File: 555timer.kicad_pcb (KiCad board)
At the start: 4 copper layers, 10 parts, among them U1 NE555P

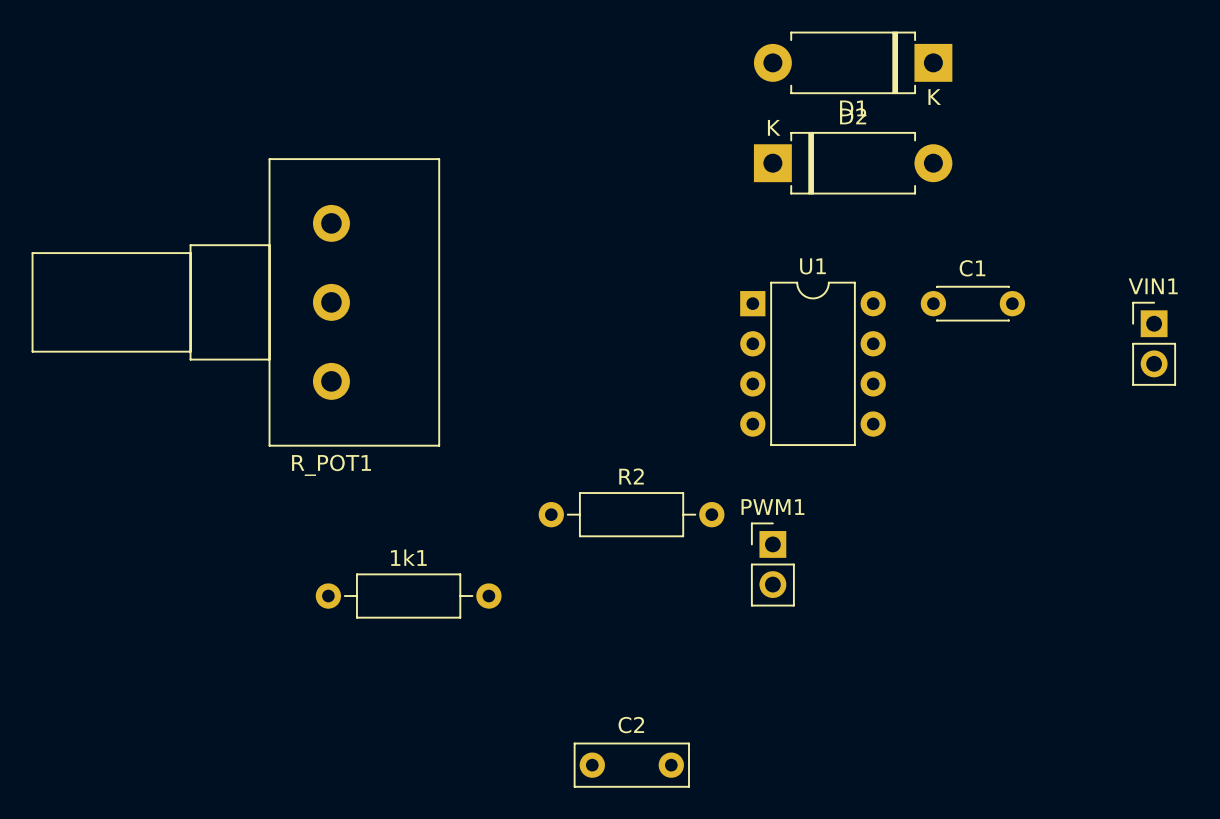
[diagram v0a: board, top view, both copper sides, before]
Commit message: Set the componnets and created a pcb rectangle
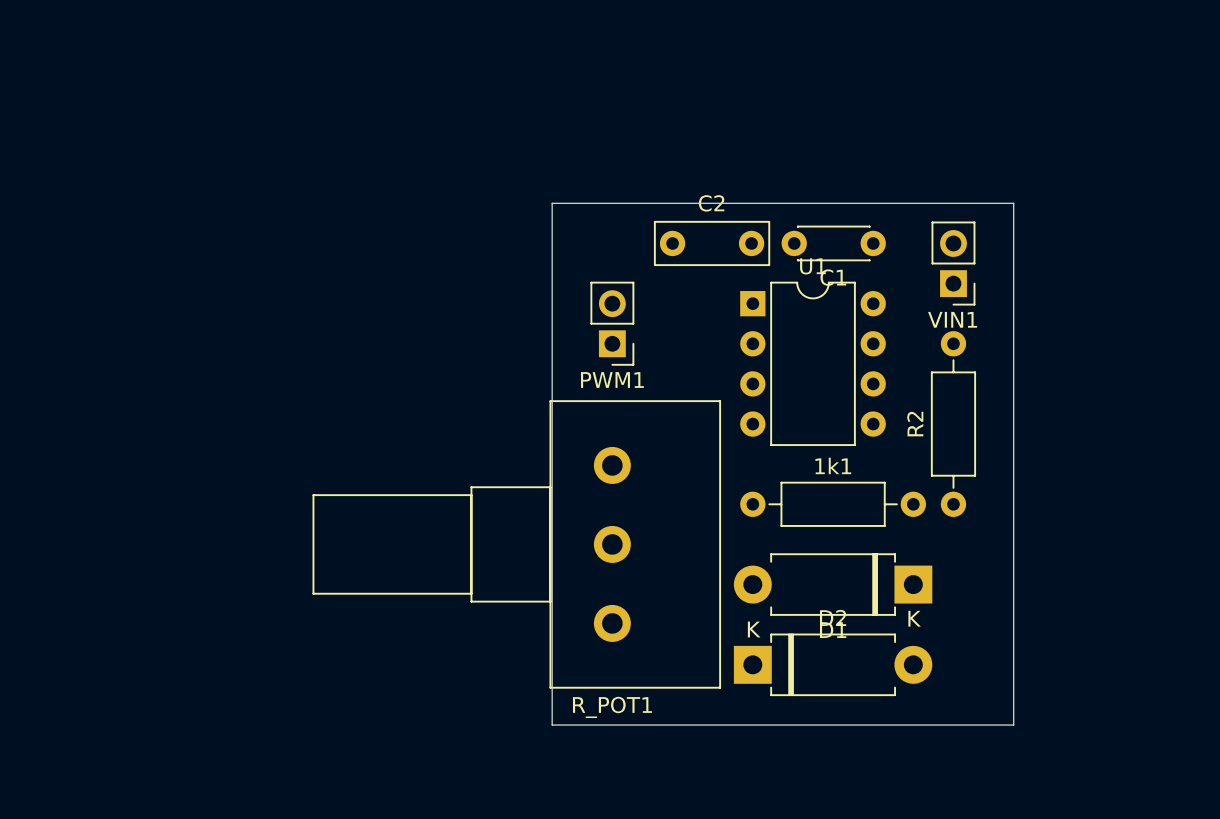
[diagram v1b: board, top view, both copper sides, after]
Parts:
- moved C2 33.4 mm to (146.1, 88.9)
- moved D1 33.0 mm to (161.3, 110.5)
- moved D2 31.8 mm to (151.1, 115.6)
- moved 1k1 27.5 mm to (151.1, 105.4)
- moved R2 25.5 mm to (163.8, 105.4), turned to 90 degrees
- moved R_POT1 23.5 mm to (142.2, 103.0)
- moved PWM1 16.3 mm to (142.2, 95.2), turned to 180 degrees
- moved VIN1 13.0 mm to (163.8, 91.4), turned to 180 degrees
- moved C1 5.39 mm to (158.8, 88.9), turned to 180 degrees
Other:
- board outline added: 29.2 x 33 mm

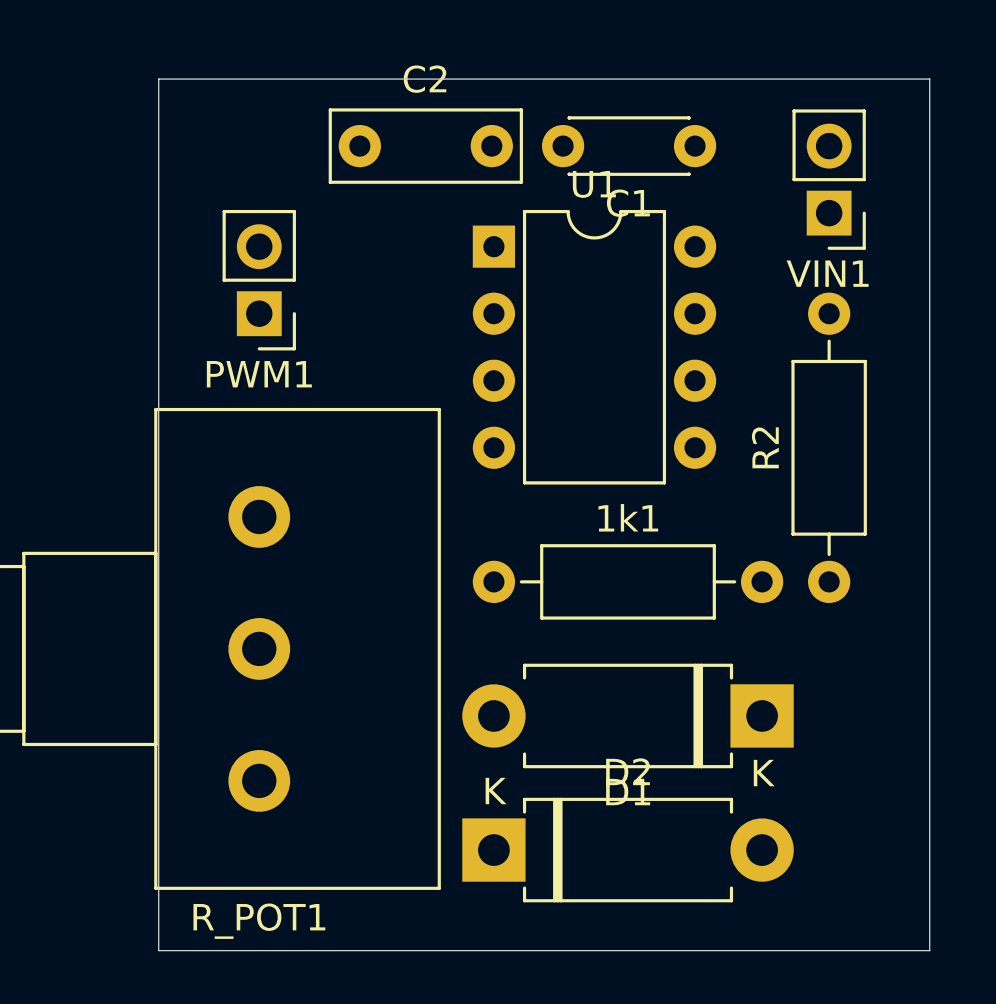
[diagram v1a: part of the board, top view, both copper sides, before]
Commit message: Rounded the corners
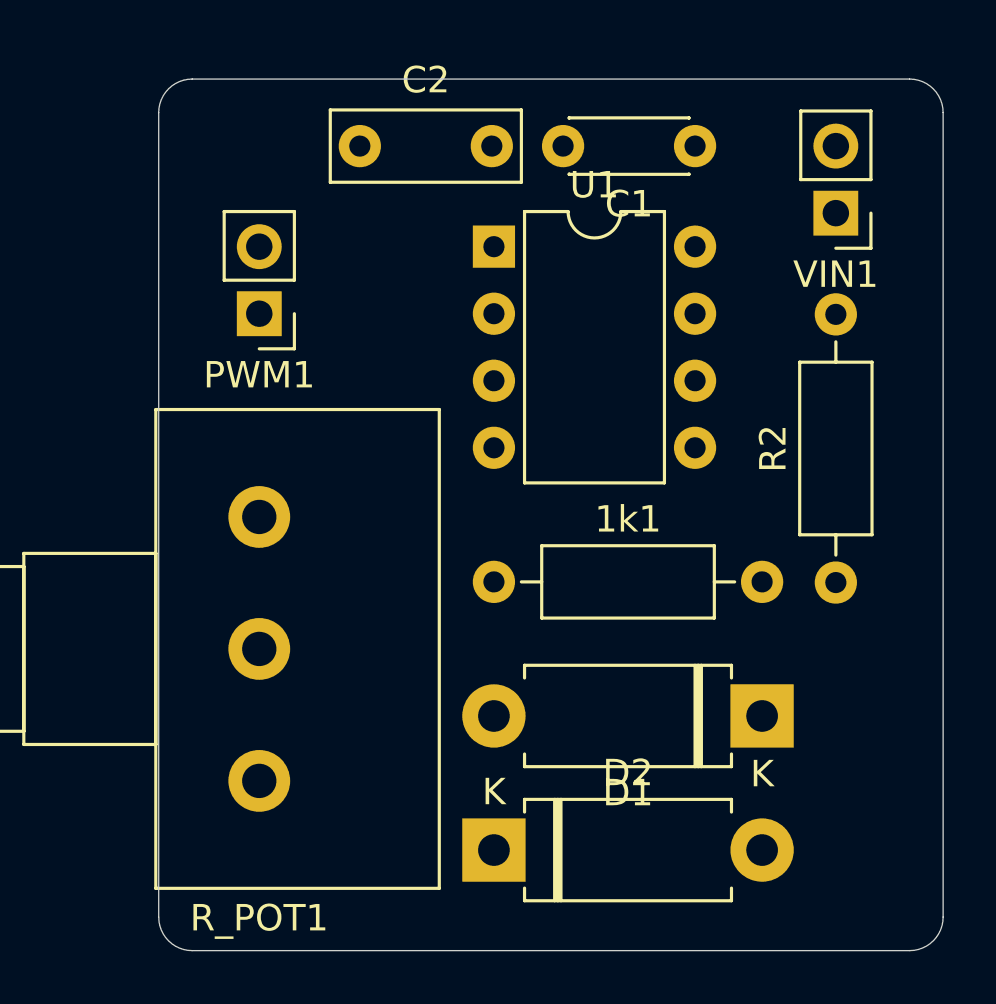
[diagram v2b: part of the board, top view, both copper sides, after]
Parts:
- moved R2 0.26 mm to (164.1, 105.4)
- moved VIN1 0.25 mm to (164.1, 91.4)
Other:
- board size 29.2 x 33 mm -> 29.7 x 33 mm
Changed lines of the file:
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@@
   (general
     (thickness 1.6002)
-    (drawings 4)
+    (drawings 8)
     (tracks 0)
     (zones 0)
@@
   )
   (module Connector_PinHeader_2.54mm:PinHeader_1x02_P2.54mm_Vertical (layer Front)
-    (at 163.83 91.44 180)
+    (at 164.084 91.44 180)
     (descr "Through hole straight pin header, 1x02, 2.54mm pitch, single row")
     (tags "Through hole pin header THT 1x02 2.54mm single row")
@@
   )
   (module Resistor_THT:R_Axial_DIN0207_L6.3mm_D2.5mm_P10.16mm_Horizontal (layer Front)
-    (at 163.83 105.41 90)
+    (at 164.084 105.4354 90)
     (descr "Resistor, Axial_DIN0207 series, Axial, Horizontal, pin pitch=10.16mm, 0.25W = 1/4W, length*diameter=6.3*2.5mm^2, http://cdn-reichelt.de/documents/datenblatt/B400/1_4W%23YAG.pdf")
     (tags "Resistor Axial_DIN0207 series Axial Horizontal pin pitch 10.16mm 0.25W = 1/4W length 6.3mm diameter 2.5mm")
@@
     )
   )
-  (gr_line (start 167.64 86.36) (end 138.43 86.36) (layer Edge.Cuts) (width 0.0254))
-  (gr_line (start 167.64 119.38) (end 167.64 86.36) (layer Edge.Cuts) (width 0.0254))
-  (gr_line (start 138.43 119.38) (end 167.64 119.38) (layer Edge.Cuts) (width 0.0254))
-  (gr_line (start 138.43 86.36) (end 138.43 119.38) (layer Edge.Cuts) (width 0.0254))
+  (gr_arc (start 139.7 87.63) (end 139.7 86.36) (angle -90) (layer Edge.Cuts) (width 0.0254))
+  (gr_arc (start 166.878 87.63) (end 168.148 87.63) (angle -90) (layer Edge.Cuts) (width 0.0254))
+  (gr_arc (start 139.7 118.11) (end 138.43 118.11) (angle -90) (layer Edge.Cuts) (width 0.0254))
+  (gr_arc (start 166.878 118.11) (end 166.878 119.38) (angle -90) (layer Edge.Cuts) (width 0.0254))
+  (gr_line (start 166.878 86.36) (end 139.7 86.36) (layer Edge.Cuts) (width 0.0254))
+  (gr_line (start 168.148 118.11) (end 168.148 87.63) (layer Edge.Cuts) (width 0.0254))
+  (gr_line (start 139.7 119.38) (end 166.878 119.38) (layer Edge.Cuts) (width 0.0254))
+  (gr_line (start 138.43 87.63) (end 138.43 118.11) (layer Edge.Cuts) (width 0.0254))
 )

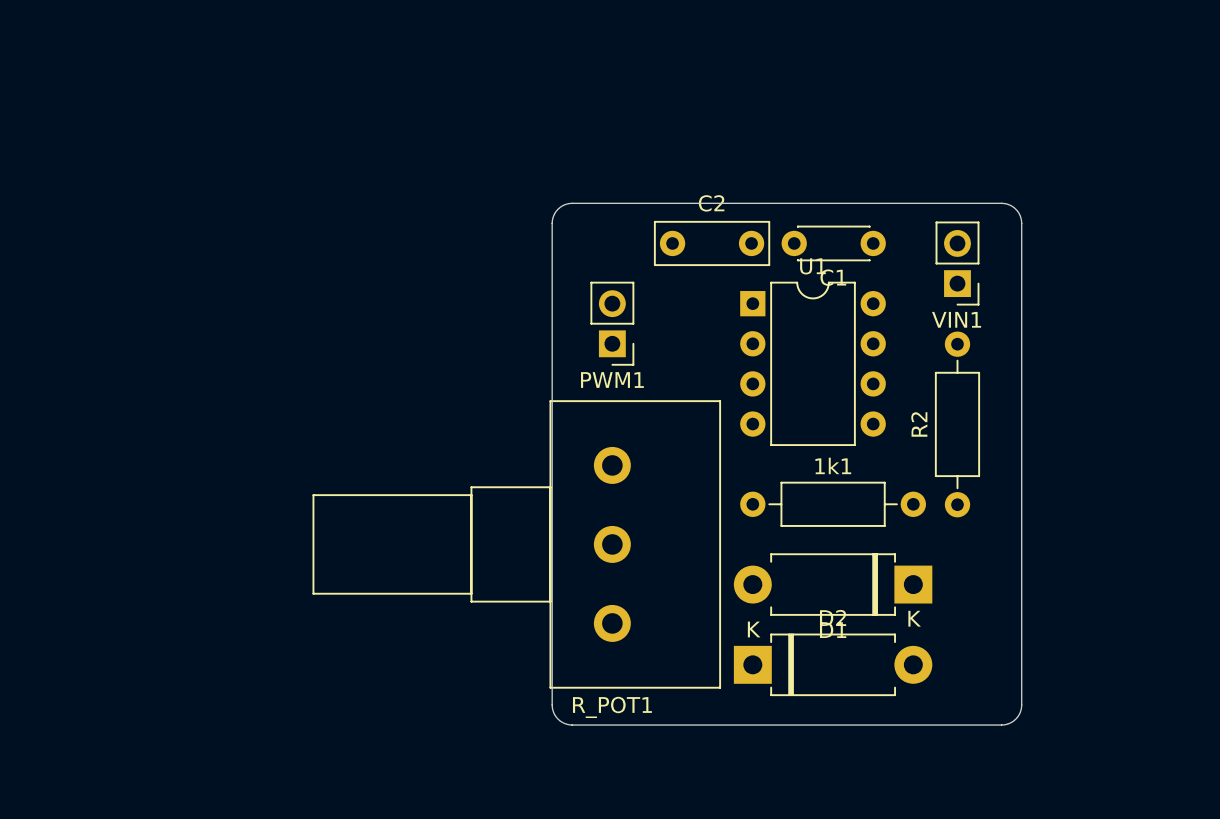
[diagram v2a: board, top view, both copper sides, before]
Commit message: Added all the traces, power planes and rearenged the silkscreen text
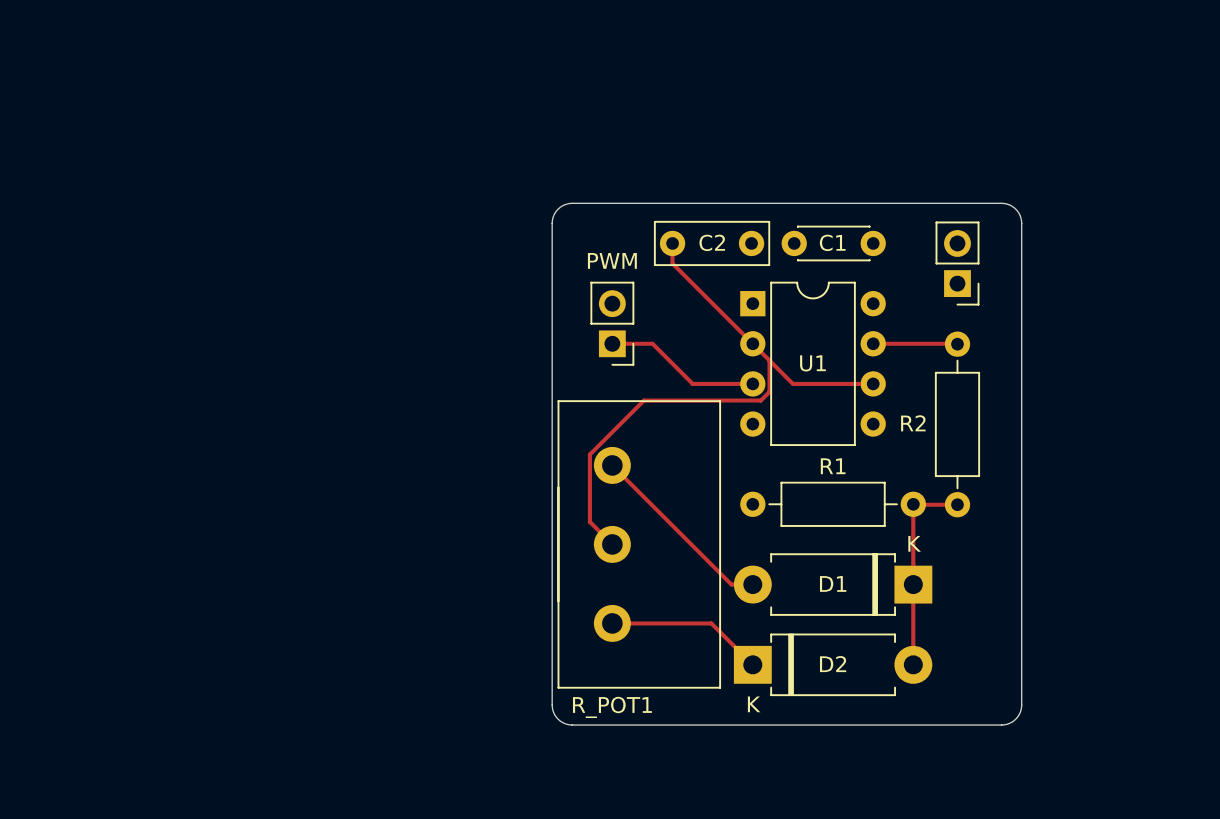
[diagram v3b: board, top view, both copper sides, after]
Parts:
- PWM: renamed from PWM1; value Conn_01x02_Female -> PWM
- R1: renamed from 1k1; value R1 -> 1k
- renumbered VIN1 to IN
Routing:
- net Net-(C2-Pad1): track 0.00 -> 38.5 mm
- net Net-(D1-Pad1): track 0.00 -> 13.0 mm
- net Net-(D1-Pad2): track 0.00 -> 12.0 mm
- net Net-(D2-Pad1): track 0.00 -> 9.98 mm
- net VDC: track 0.00 -> 9.94 mm
- net Net-(R2-Pad2): track 0.00 -> 5.34 mm
- added copper zone on In1.Cu, net GND
- added copper zone on In2.Cu, net VCC
